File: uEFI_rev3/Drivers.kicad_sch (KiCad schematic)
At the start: 28 parts, among them Q1 ISL9V5045S3ST, Q2 ISL9V5045S3ST, Q3 ISL9V5045S3ST, Q4 ISL9V5045S3ST

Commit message: rev3, analog inputs
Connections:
- net M3: now also C29.2; no longer C30.2
- net M4: now also C30.2; no longer C29.2
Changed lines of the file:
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@@
     )
   )
-  (global_label "M3" (shape input) (at 165.1 147.32 0)
+  (global_label "M3" (shape input) (at 165.1 149.86 0)
+    (effects (font (size 1.27 1.27)) (justify left))
+    (property "Intersheet References" "${INTERSHEET_REFS}" (id 0) (at 170.1741 149.7806 0)
+      (effects (font (size 1.27 1.27)) (justify left) hide)
+    )
+  )
+  (global_label "M4" (shape input) (at 165.1 147.32 0)
     (effects (font (size 1.27 1.27)) (justify left))
     (property "Intersheet References" "${INTERSHEET_REFS}" (id 0) (at 170.1741 147.2406 0)
       (effects (font (size 1.27 1.27)) (justify left) hide)
     )
-  )
-  (global_label "M4" (shape input) (at 165.1 149.86 0)
-    (effects (font (size 1.27 1.27)) (justify left))
-    (property "Intersheet References" "${INTERSHEET_REFS}" (id 0) (at 170.1741 149.7806 0)
-      (effects (font (size 1.27 1.27)) (justify left) hide)
-    )

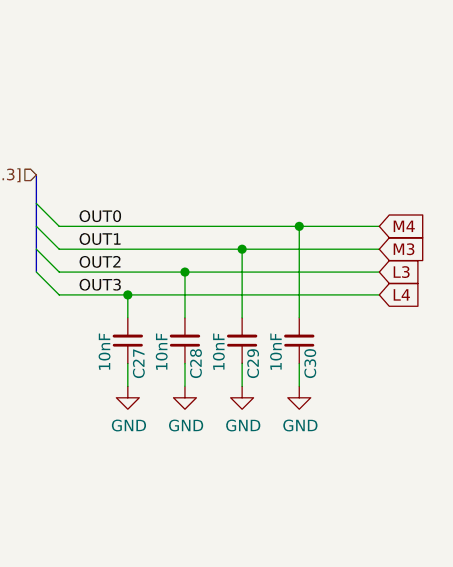
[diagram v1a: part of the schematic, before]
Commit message: rev3, connect PMIC to injector outs
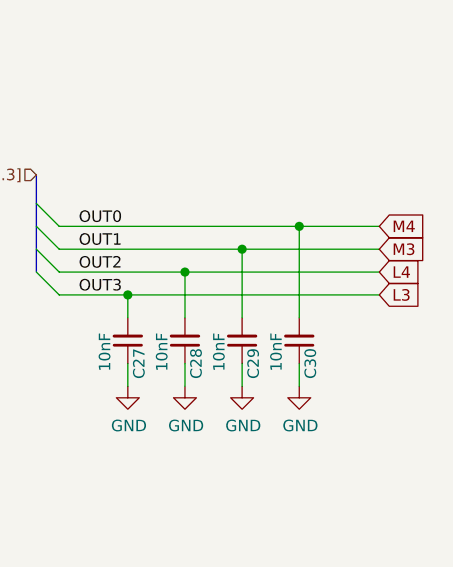
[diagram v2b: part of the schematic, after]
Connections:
- net L3: now also C27.2; no longer C28.2
- net L4: now also C28.2; no longer C27.2
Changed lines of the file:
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@@
     (effects (font (size 1.27 1.27)) (justify right bottom))
   )
-  (global_label "L3" (shape input) (at 165.1 152.4 0)
+  (global_label "L3" (shape input) (at 165.1 154.94 0)
+    (effects (font (size 1.27 1.27)) (justify left))
+    (property "Intersheet References" "${INTERSHEET_REFS}" (id 0) (at 169.7507 154.8606 0)
+      (effects (font (size 1.27 1.27)) (justify left) hide)
+    )
+  )
+  (global_label "L4" (shape input) (at 165.1 152.4 0)
     (effects (font (size 1.27 1.27)) (justify left))
     (property "Intersheet References" "${INTERSHEET_REFS}" (id 0) (at 169.7507 152.3206 0)
       (effects (font (size 1.27 1.27)) (justify left) hide)
     )
-  )
-  (global_label "L4" (shape input) (at 165.1 154.94 0)
-    (effects (font (size 1.27 1.27)) (justify left))
-    (property "Intersheet References" "${INTERSHEET_REFS}" (id 0) (at 169.7507 154.8606 0)
-      (effects (font (size 1.27 1.27)) (justify left) hide)
-    )
